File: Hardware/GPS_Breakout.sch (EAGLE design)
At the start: 8 parts, among them U1 JST_VERTICAL

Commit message: Production ready!
Added fiducials for manufacture. Panelized into production matrix.
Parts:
- added FID1, FID2: FIDUCIALUFIDUCIAL, SparkFun-Aesthetics:FIDUCIALUFIDUCIAL
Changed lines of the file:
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@@
 <?xml version="1.0" encoding="utf-8"?>
 <!DOCTYPE eagle SYSTEM "eagle.dtd">
-<eagle version="6.4">
+<eagle version="6.3">
 <drawing>
 <settings>
@@
 <part name="JP2" library="SparkFun" deviceset="LOGO-SFE" device="SK"/>
 <part name="FRAME2" library="SparkFun-Aesthetics" deviceset="FRAME-LETTER" device=""/>
+<part name="FID1" library="SparkFun-Aesthetics" deviceset="FIDUCIAL" device="UFIDUCIAL"/>
+<part name="FID2" library="SparkFun-Aesthetics" deviceset="FIDUCIAL" device="UFIDUCIAL"/>
 </parts>
 <sheets>
@@
 <instance part="FRAME2" gate="G$1" x="0" y="-2.54"/>
 <instance part="FRAME2" gate="G$2" x="147.32" y="-2.54"/>
+<instance part="FID1" gate="G$1" x="233.68" y="30.48"/>
+<instance part="FID2" gate="G$1" x="233.68" y="25.4"/>
 </instances>
 <busses>

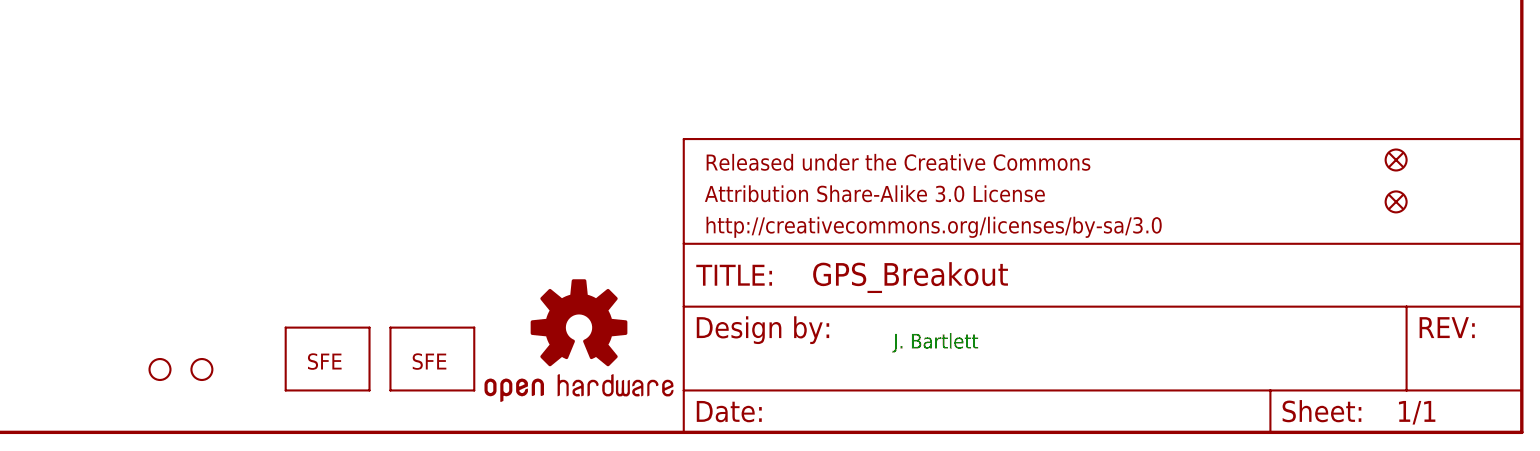
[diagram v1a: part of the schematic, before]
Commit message: Adding version number to schematic
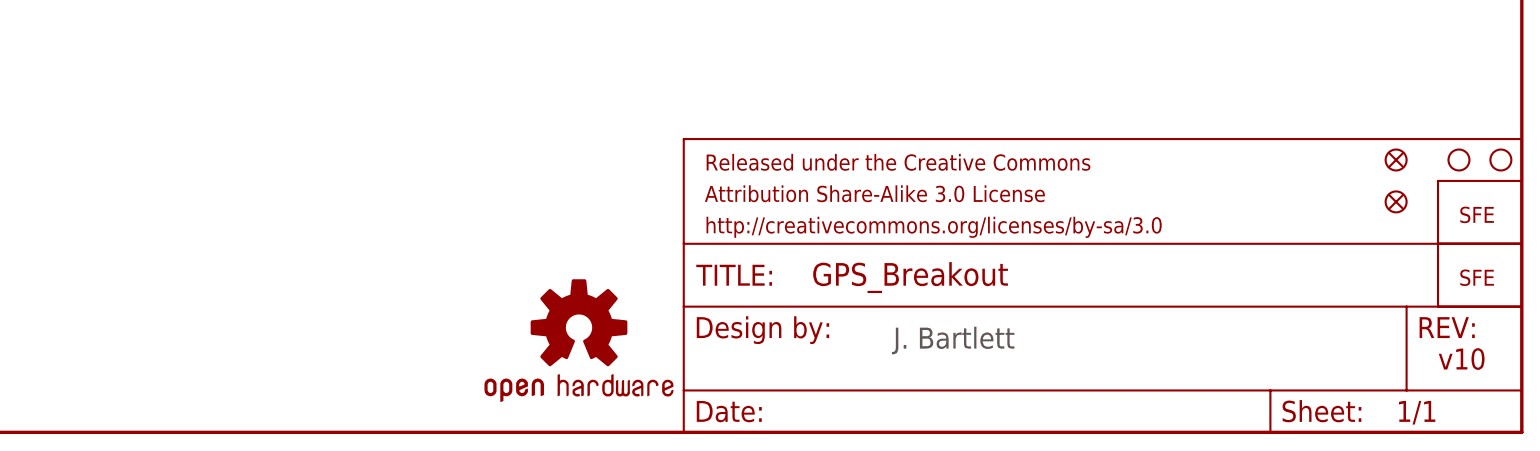
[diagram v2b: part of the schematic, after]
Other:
- note added: "v10"
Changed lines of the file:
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@@
 <?xml version="1.0" encoding="utf-8"?>
 <!DOCTYPE eagle SYSTEM "eagle.dtd">
-<eagle version="6.3">
+<eagle version="6.4">
 <drawing>
 <settings>
@@
 <sheet>
 <plain>
-<text x="172.72" y="7.62" size="1.778" layer="91">J. Bartlett</text>
+<text x="172.72" y="7.62" size="2.54" layer="97">J. Bartlett</text>
+<text x="238.76" y="5.08" size="2.54" layer="94">v10</text>
 </plain>
 <instances>
-<instance part="JP4" gate="G$1" x="83.82" y="5.08"/>
-<instance part="JP6" gate="G$1" x="88.9" y="5.08"/>
-<instance part="JP7" gate="G$1" x="114.3" y="5.08"/>
+<instance part="JP4" gate="G$1" x="246.38" y="30.48"/>
+<instance part="JP6" gate="G$1" x="241.3" y="30.48"/>
+<instance part="JP7" gate="G$1" x="241.3" y="22.86"/>
 <instance part="U1" gate="G$1" x="76.2" y="101.6" rot="R180"/>
 <instance part="JP1" gate="G$1" x="111.76" y="104.14" rot="R180"/>
 <instance part="LOGO1" gate="G$1" x="134.62" y="10.16"/>
-<instance part="JP2" gate="G$1" x="101.6" y="5.08"/>
+<instance part="JP2" gate="G$1" x="241.3" y="15.24"/>
 <instance part="FRAME2" gate="G$1" x="0" y="-2.54"/>
 <instance part="FRAME2" gate="G$2" x="147.32" y="-2.54"/>
